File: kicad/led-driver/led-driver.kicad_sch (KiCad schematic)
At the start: 37 parts, among them J1 RJ45, J10 Conn_02x06_Odd_Even, J11 Conn_02x06_Odd_Even, J2 RJ45, J3 Conn_01x02_Pin, J4 Conn_02x06_Odd_Even, J5 Conn_02x06_Odd_Even, J6 Conn_02x06_Odd_Even, J7 Conn_02x06_Odd_Even, J8 Conn_02x06_Odd_Even, J9 Conn_02x06_Odd_Even, U1 LP2985-33DBVR, U2 SN65LVDS049, U3 TLC5971PWP

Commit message: Progress
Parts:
- renumbered D12 to D1, D3 to D10, D2 to D11, D1 to D12, D11 to D2, D10 to D3, D9 to D4, D8 to D5, D7 to D6, D6 to D7, D5 to D8, D4 to D9
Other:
- moved on the sheet: D1, D10, D11, D12, D2, D3, D4, D5, D6, D7, D8, D9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

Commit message: Add testpoints to pcbs
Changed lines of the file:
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@@
 (kicad_sch
-	(version 20231120)
+	(version 20250114)
 	(generator "eeschema")
-	(generator_version "8.0")
+	(generator_version "9.0")
 	(paper "A4")
 	(junction
@@
 		)
 	)
+	(embedded_fonts no)
 )

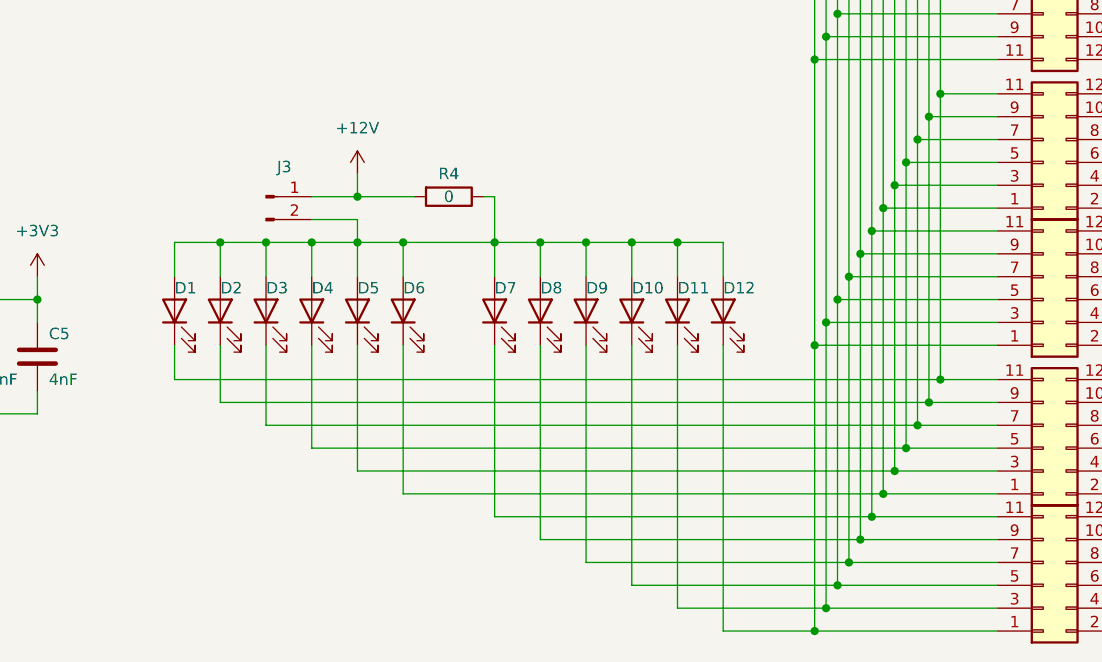
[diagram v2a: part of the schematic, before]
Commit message: Fix led enumeration
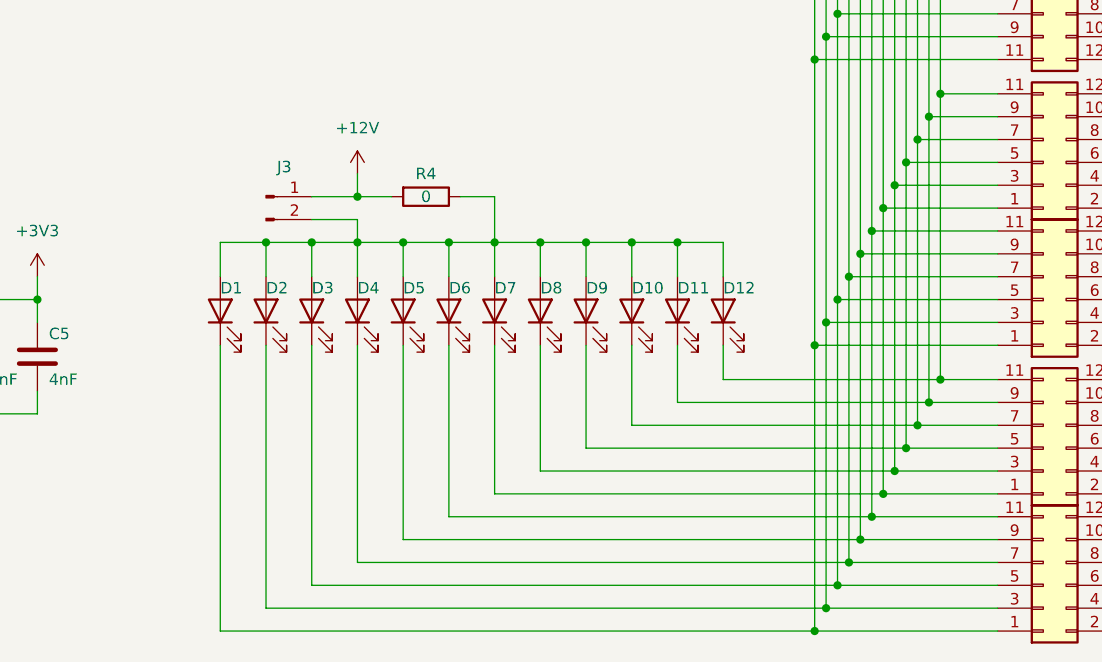
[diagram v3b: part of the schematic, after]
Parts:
- renumbered D12 to D1, D3 to D10, D2 to D11, D1 to D12, D11 to D2, D10 to D3, D9 to D4, D8 to D5, D7 to D6, D6 to D7, D5 to D8, D4 to D9
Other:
- moved on the sheet: D1, D10, D11, D12, D2, D3, D4, D5, D6, D7, D8, D9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
